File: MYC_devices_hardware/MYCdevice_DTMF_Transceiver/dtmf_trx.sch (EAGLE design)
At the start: 40 parts, among them IC1 MEGA8-P, IC2 MAX232, IC4 CM8870CP, IC5 78L05Z, Q1 20MHz, Q2 3,579545MHz, X1 8-15V, X2 1503_09, X3 1503_09, X4 RS232

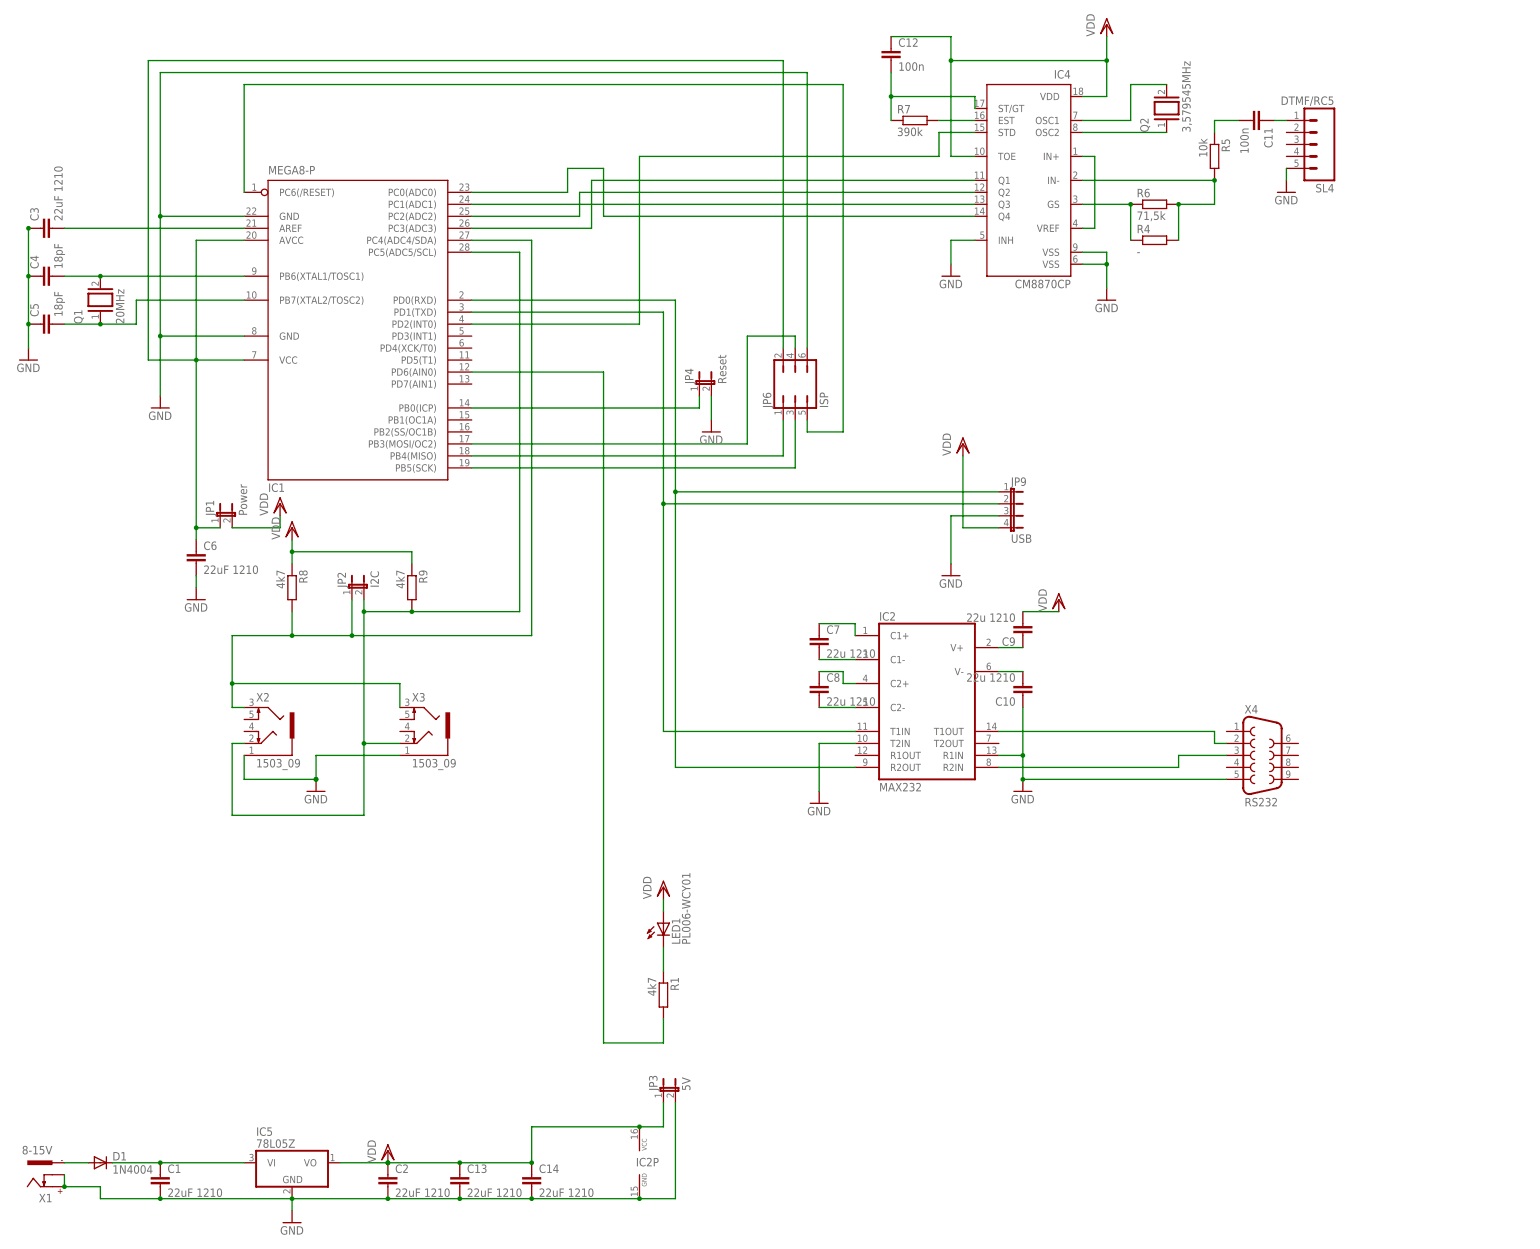
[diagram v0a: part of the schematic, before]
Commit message: DTMF TRX (MT8880) added
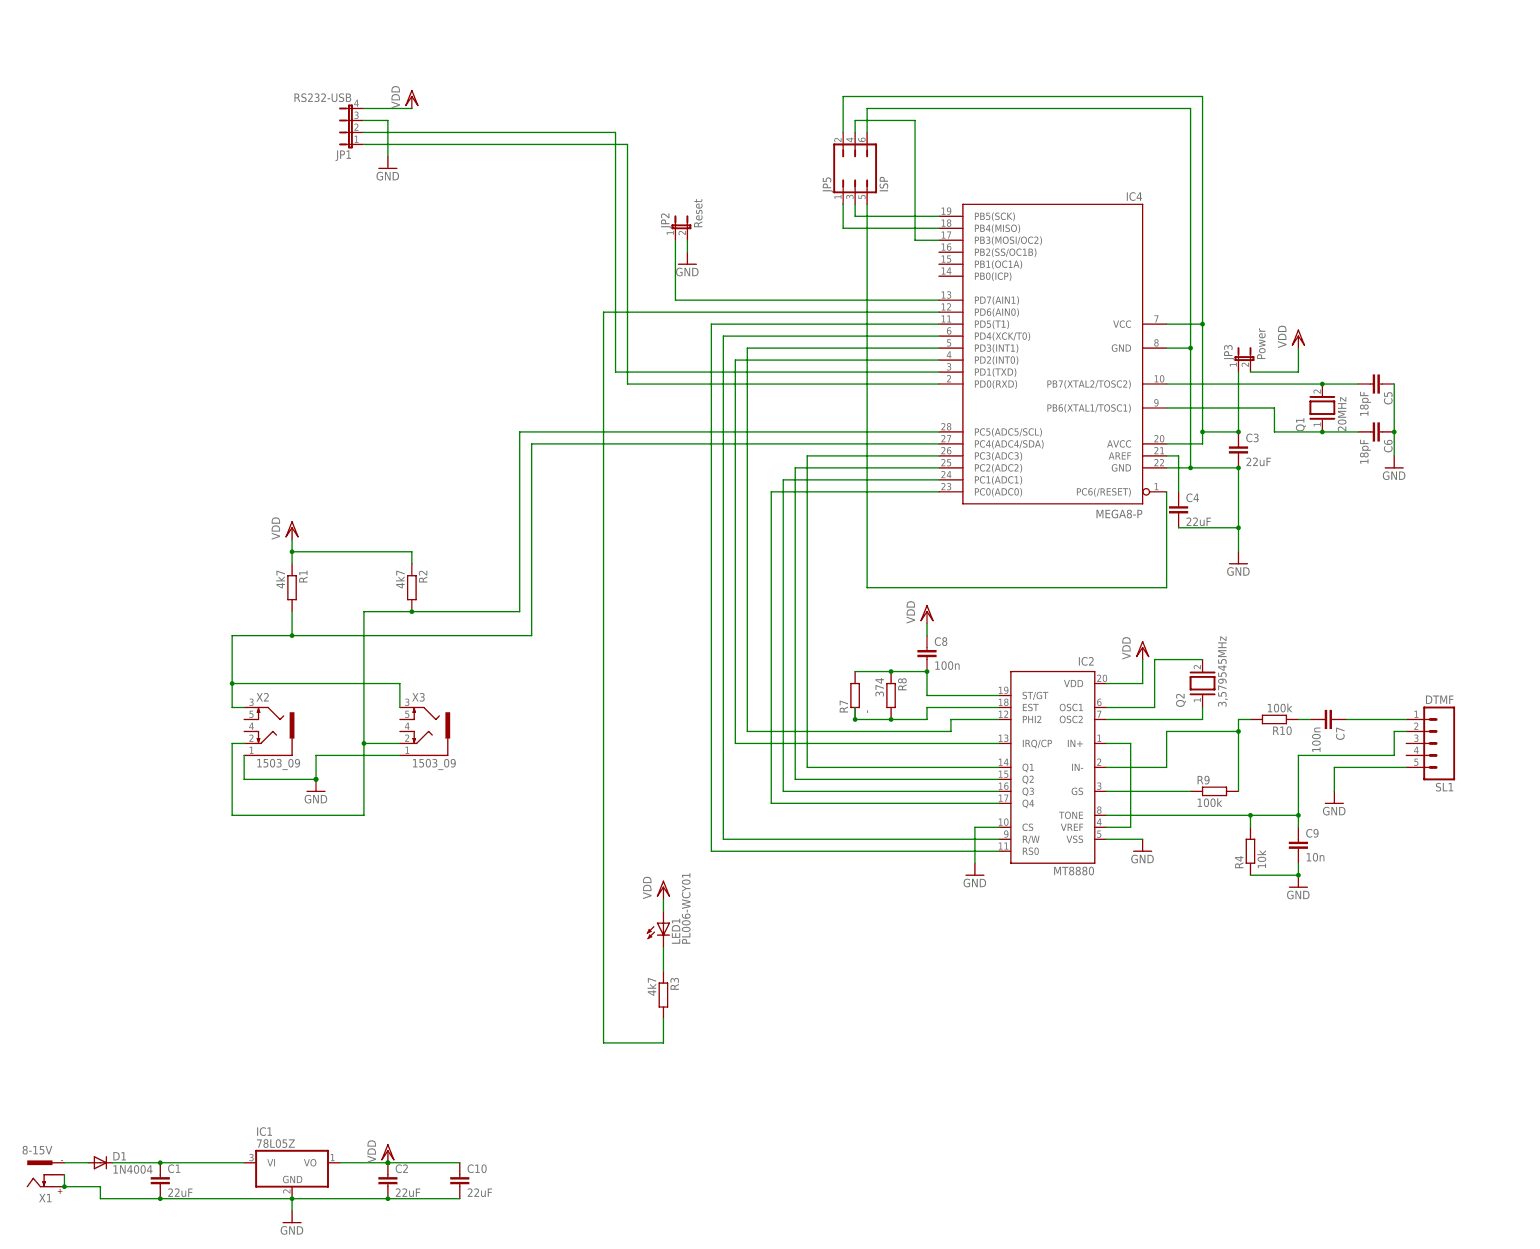
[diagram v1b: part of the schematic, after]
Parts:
- removed C11, C12: 100n, rcl:C-EU050-025X075
- removed C13, C14: 22uF 1210, rcl:C-EUC1206
- removed IC5: 78L05Z, linear:78L05Z
- removed JP4: Reset, jumper:JP1E
- removed JP6: ISP, jumper:JP3Q
- removed JP9: USB, jumper:JP4E
- removed R5: 10k, resistor:R-EU_0207/5V
- removed R6: 71,5k, resistor:R-EU_0207/5V
- removed SL4: DTMF/RC5, con-amp-quick:M05
- removed X4: RS232, con-subd:F09H
- added JP5: ISP, jumper:JP3Q
- added R10: 100k, resistor:R-EU_0207/5V
- added R2: 4k7, resistor:R-EU_0207/5V
- added R3: 4k7, resistor:R-EU_M1206
- added SL1: DTMF, con-amp-quick:M05
- C1, C2, C3: value 22uF 1210 -> 22uF
- C10: value 22u 1210 -> 22uF
- C4: value 18pF -> 22uF; device resistor:C-EU025-025X050 -> rcl:C-EUC1206
- C6: value 22uF 1210 -> 18pF; device rcl:C-EUC1206 -> resistor:C-EU025-025X050
- C7, C8: value 22u 1210 -> 100n; device rcl:C-EUC1206 -> resistor:C-EU050-025X075
- C9: value 22u 1210 -> 10n; device rcl:C-EUC1206 -> resistor:C-EU050-025X075
- IC1: value MEGA8-P -> 78L05Z; device atmel:MEGA8-P -> linear:78L05Z
- IC2: value MAX232 -> MT8880; device maxim:MAX232 -> dk1ri:MT8880
- IC4: value CM8870CP -> MEGA8-P; device california-micro-devices:CM8870CP -> atmel:MEGA8-P
- JP1: value Power -> RS232-USB; device jumper:JP1E -> jumper:JP4E
- JP2: value I2C -> Reset
- JP3: value 5V -> Power
- R4: value - -> 10k
- R7: value 390k -> -
- R8: value 4k7 -> 374
- R9: value 4k7 -> 100k
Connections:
- removed net C13: C7.1, IC2G$1.C1+
- removed net N$34: IC1.PC3(ADC3), IC4.Q1
- removed net N$37: C5.2, IC1.PB7(XTAL2/TOSC2), Q1.1
- removed net N$38: IC1.PC2(ADC2), IC4.Q2
- removed net N$40: C12.2, IC4.ST/GT, R7.1
- removed net N$42: IC1.PD2(INT0), IC4.STD
- removed net N$44: C6.1, IC1.AVCC, IC1.VCC@1, JP1.1, JP6.2
- removed net N$7 (its old number): IC4.IN+, IC4.VREF
- new net N$10: IC2.Q2, IC4.PC2(ADC2)
- new net N$27: IC4.PD0(RXD), JP1.1
- new net N$58: C3.1, IC4.AVCC, IC4.VCC@1, JP3.1, JP5.2
- new net N$9: IC2.Q3, IC4.PC1(ADC1)
- net GND: now also C10.2, C3.2, C4.2, C6.1, C9.2, IC2.CS, IC2.VSS, IC4.GND, IC4.GND@1, JP1.3, JP2.2, JP5.6, R4.1, SL1.5; no longer C10.1, C13.2, C14.2, C3.1, C4.1, C6.2, IC1.GND@1, IC2G$1.R1IN, IC2G$1.T2IN, IC2P.GND, IC4.INH, IC4.VSS, IC4.VSS@1, IC5.GND, JP3.2, JP4.2, JP6.6, JP9.3, SL4.5, X4.5
- net N$1: now also IC4.PD6(AIN0), R3.2; no longer IC1.PD6(AIN0), R1.2
- net N$11: now also IC2.Q1, IC4.PC3(ADC3); no longer IC2G$1.R2IN, X4.3
- net N$12: now also IC2.PHI2, IC4.PD3(INT1); no longer IC1.PD1(TXD), IC2G$1.T1IN, JP9.2
- net N$13: now also IC2.OSC1, Q2.2; no longer C8.1, IC2G$1.C2+
- net N$14: now also IC2.OSC2, Q2.1; no longer C7.2, IC2G$1.C1-
- net N$15: now also IC4.PB3(MOSI/OC2), JP5.4; no longer IC1.PB4(MISO), JP6.1
- net N$16: now also IC2.IN+, IC2.VREF; no longer C9.1, IC2G$1.V+
- net N$17: now also C7.1, SL1.1; no longer C10.2, IC2G$1.V-
- net N$18: now also IC4.PC6(/RESET), JP5.5; no longer IC1.PC6(/RESET), JP6.5
- net N$19: now also C5.2, IC4.PB7(XTAL2/TOSC2); no longer C4.2, IC1.PB6(XTAL1/TOSC1)
- net N$2: now also IC2.RS0, IC4.PD5(T1); no longer IC1.PD0(RXD), IC2G$1.R2OUT, JP9.1
- net N$20: now also IC4.PB4(MISO), JP5.1; no longer IC1.PB5(SCK), JP6.3
- net N$21: now also C7.2, R10.1; no longer C11.1, SL4.1
- net N$22: now also IC4.PC5(ADC5/SCL), R2.2; no longer IC1.PC5(ADC5/SCL), JP2.2, R9.2
- net N$24: now also IC2.IN-, R10.2, R9.2; no longer C11.2, R5.1
- net N$25: now also C8.2, IC2.ST/GT, R7.2, R8.1; no longer IC4.IN-, R4.2, R5.2, R6.2
- net N$26: now also C6.2, IC4.PB6(XTAL1/TOSC1), Q1.1; no longer IC4.GS, R4.1, R6.1
- net N$28: now also IC4.PB5(SCK), JP5.3; no longer IC1.PB3(MOSI/OC2), JP6.4
- net N$29: now also IC2.GS, R9.1; no longer IC4.OSC2, Q2.1
- net N$3: now also IC2.R/W, IC4.PD4(XCK/T0); no longer C8.2, IC2G$1.C2-
- net N$30: now also C9.1, IC2.TONE, R4.2, SL1.2; no longer IC1.PC1(ADC1), IC4.Q3
- net N$31: now also IC2.EST, R7.1, R8.2; no longer IC4.OSC1, Q2.2
- net N$32: now also C4.1, IC4.AREF; no longer IC4.EST, R7.2
- net N$33: now also IC1.VI; no longer IC5.VI
- net N$35: now also IC4.PD1(TXD), JP1.2; no longer C3.2, IC1.AREF
- net N$4: now also IC2.IRQ/CP, IC4.PD2(INT0); no longer IC2G$1.T1OUT, X4.2
- net N$5: now also IC4.PC4(ADC4/SDA), R1.2; no longer IC1.PC4(ADC4/SDA), JP2.1, R8.2
- net N$50: now also R3.1; no longer R1.1
- net N$6: now also IC4.PD7(AIN1), JP2.1; no longer IC1.PB0(ICP), JP4.1
- net N$8: now also IC2.Q4, IC4.PC0(ADC0); no longer IC1.PC0(ADC0), IC4.Q4
- net VDD: now also C10.1, C8.1, IC1.VO, IC2.VDD, JP1.4, JP3.2, R1.1, R2.1; no longer C12.1, C13.1, C14.1, C9.2, IC2P.VCC, IC4.TOE, IC4.VDD, IC5.VO, JP1.2, JP3.1, JP9.4, R8.1, R9.1
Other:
- moved on the sheet: C10, C3, C4, C5, C6, C7, C8, C9, JP2, JP3, Q1, Q2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
